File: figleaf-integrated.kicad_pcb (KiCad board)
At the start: 2 copper layers, 145 x 106 mm, 70 parts, among them J1 Conn_01x02_Pin, J2 HRO_TYPE-C-31-M-14, J3 Battery, J9 TC2030_SWD, Q2 2N7002, SW1 PWR, SW2 RST, U1 SRV05-4, U10 MAX17048, U3 BQ24075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

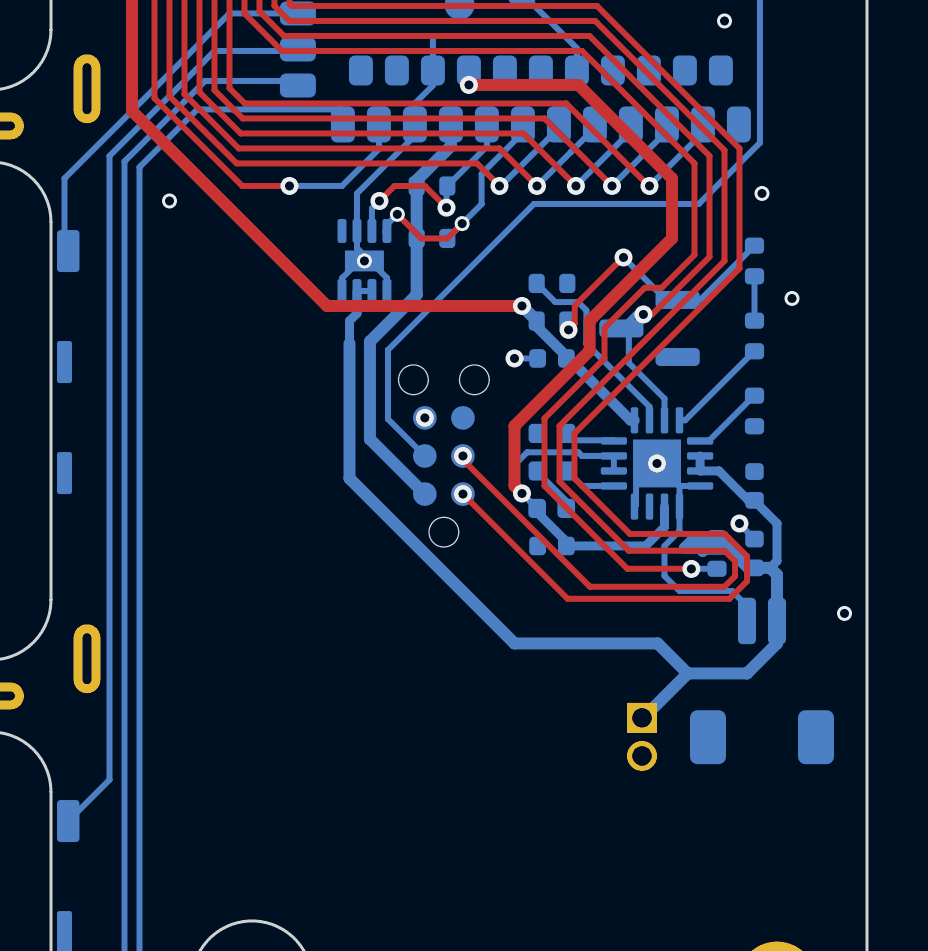
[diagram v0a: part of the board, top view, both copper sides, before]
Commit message: move batt conn
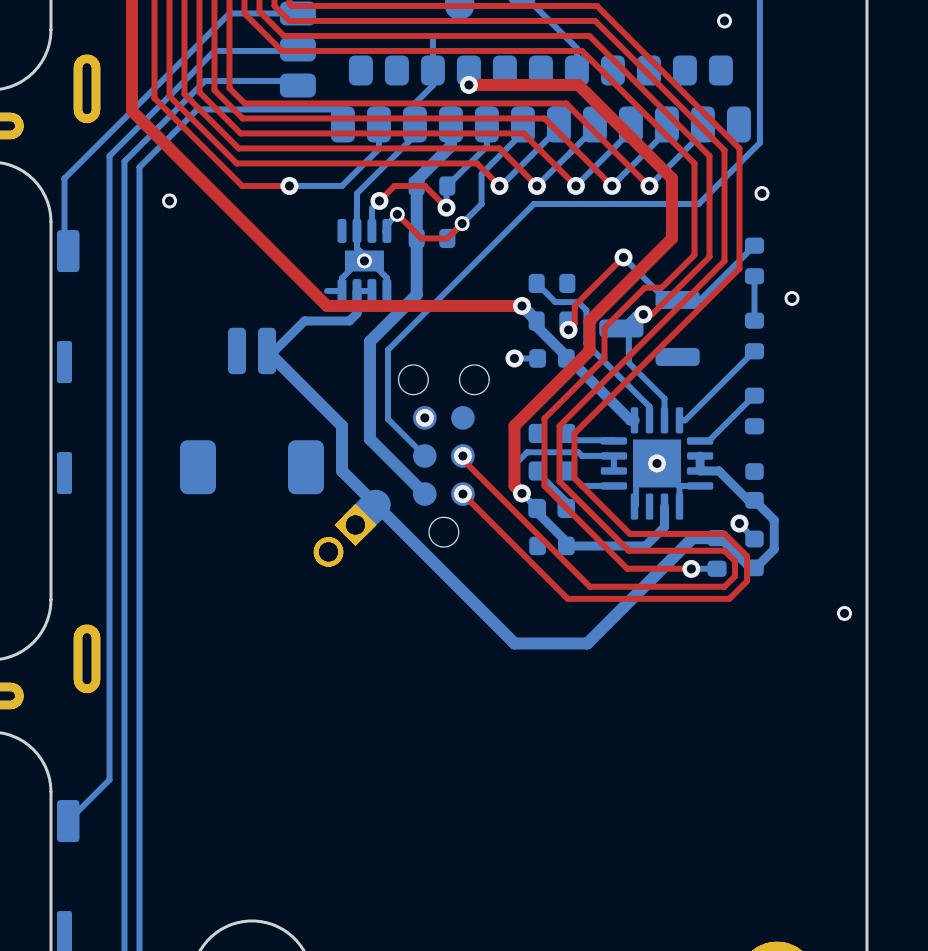
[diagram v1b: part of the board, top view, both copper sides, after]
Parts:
- moved J3 19.2 mm to (137.0, 46.0)
- moved J1 11.5 mm to (140.4, 49.8), turned to -45 degrees
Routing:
- net +BATT: track 40.9 -> 34.3 mm
- net GND_L: track 30.2 -> 24.5 mm

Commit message: move pwr and rst SW
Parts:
- moved SW2 2.75 mm to (124.0, 14.0)
- moved SW1 1.75 mm to (133.0, 14.2)
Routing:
- net RST: track 67.4 -> 70.1 mm
- net Net-(SW1-A): track 56.4 -> 57.9 mm
- net SYSOFF: track 45.4 -> 46.2 mm

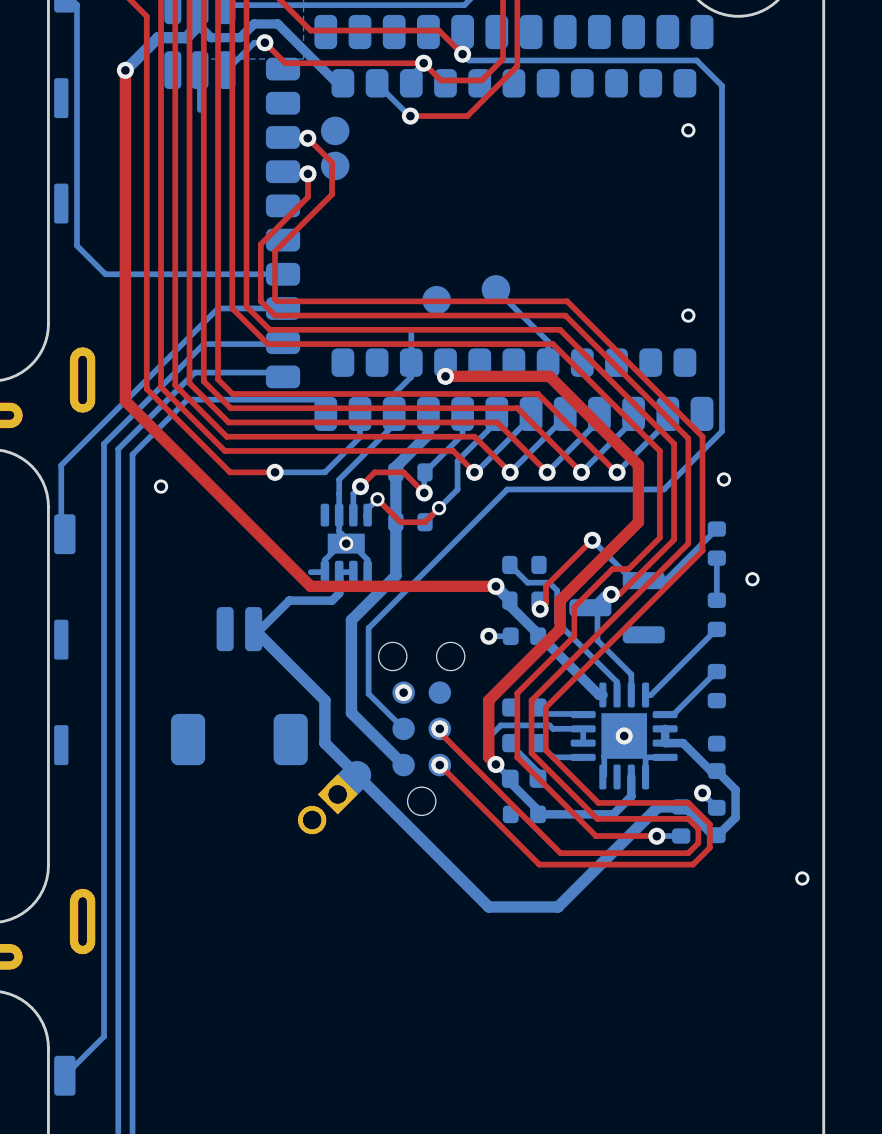
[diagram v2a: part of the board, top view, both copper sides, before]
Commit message: move +B conn
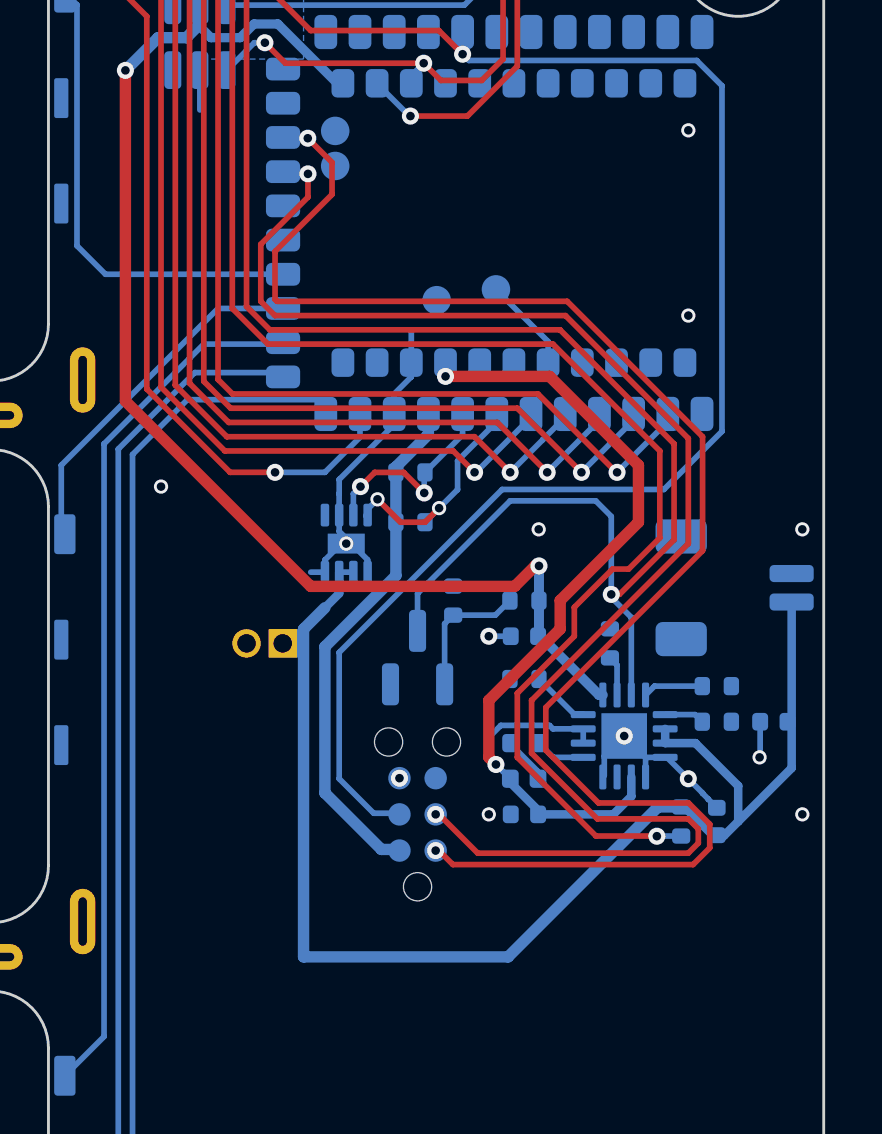
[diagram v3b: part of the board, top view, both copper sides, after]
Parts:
- moved J3 17.7 mm to (154.4, 42.5), turned to 90 degrees
- moved R7 9.46 mm to (144.5, 43.0), turned to 90 degrees
- moved Q2 7.22 mm to (143.2, 45.0), turned to 90 degrees
- moved J1 5.64 mm to (138.5, 44.5), turned to -90 degrees
- moved R11 4.07 mm to (150.0, 44.5), turned to 90 degrees
- moved J9 3.00 mm to (143.2, 50.5)
- moved R13 2.50 mm to (153.8, 46.0), turned to 0 degrees
- moved C7 2.36 mm to (155.8, 47.2), turned to 180 degrees
- moved R9 1.25 mm to (153.8, 47.2), turned to 0 degrees
- moved R12 1.00 mm to (147.0, 45.8)
- turned R4 to 180 degrees
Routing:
- net SYSOFF: track 46.2 -> 58.2 mm
- net +BATT: track 34.3 -> 46.0 mm
- net /TMR: track 6.57 -> 1.41 mm
- net RST: track 70.1 -> 74.5 mm
- net Net-(Q2-G): track 8.89 -> 4.82 mm, vias 2 -> 0
- net +3.3V: track 14.2 -> 18.3 mm
- net +5V: track 46.6 -> 48.6 mm
- net GND_L: track 24.5 -> 26.2 mm, vias 17 -> 19
- net Net-(U3-ISET): track 3.45 -> 2.12 mm
- net SWDIO: track 56.8 -> 55.6 mm
- net SWDCLK: track 54.9 -> 53.8 mm
- net Net-(U3-TS): track 2.44 -> 1.41 mm

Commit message: Fix DRC
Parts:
- moved J1 0.48 mm to (139.0, 44.5)
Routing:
- net GND_L: track 26.2 -> 41.8 mm
- net +BATT: track 46.0 -> 42.0 mm

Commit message: cleanup
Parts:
- moved U10 0.58 mm to (140.2, 41.0)
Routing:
- net SCL: track 7.18 -> 7.75 mm
- net col_2: track 108.4 -> 107.9 mm

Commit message: cleanup
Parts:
- moved R11 0.64 mm to (149.4, 44.5), turned to 135 degrees
- moved C7 0.25 mm to (156.0, 47.2)
- moved R13 0.25 mm to (154.0, 46.0)
- moved R9 0.25 mm to (154.0, 47.2)

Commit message: move RST
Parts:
- moved SW2 0.25 mm to (124.0, 13.8)
